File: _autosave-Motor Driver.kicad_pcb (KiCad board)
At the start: 2 copper layers, 103.6 x 67.8 mm, 45 parts, among them CON1 AVR-ISP-6, J1 Conn_01x02, J10 Conn_01x04, J2 Conn_01x02, J3 Conn_01x04, J4 Conn_01x04, J5 Conn_01x04, J6 Conn_02x02_Odd_Even, J7 Conn_01x02, J8 Conn_01x02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

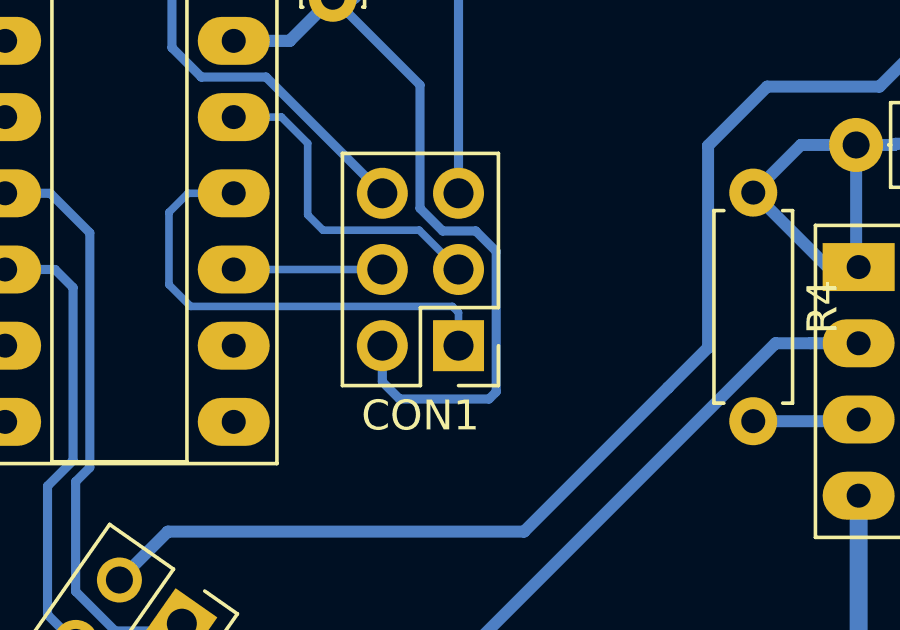
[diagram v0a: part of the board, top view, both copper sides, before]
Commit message: Updated SCH|PCB
Updated the SCh for polarity change on the fly using the 2x2 pinheader
PCB was completely newly designed
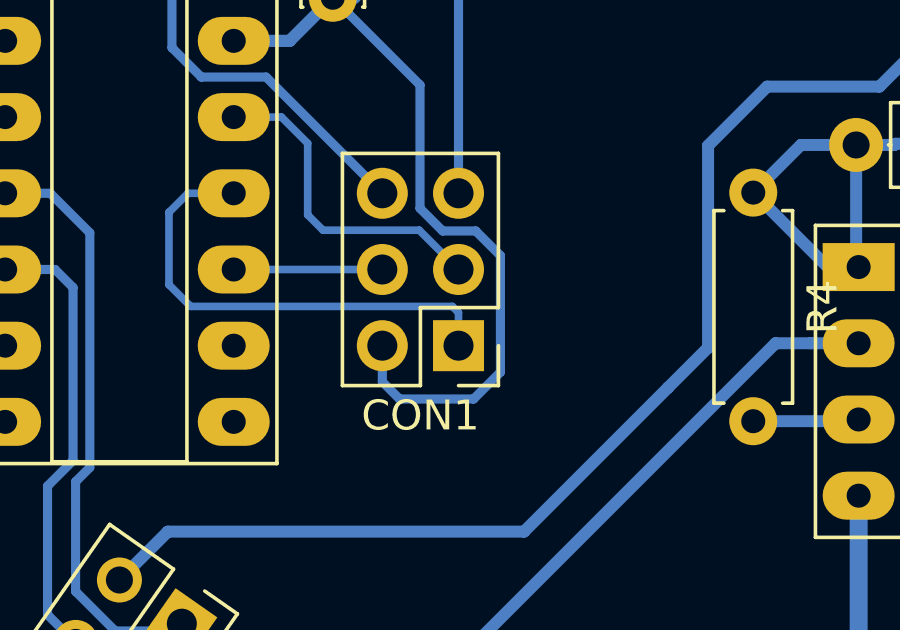
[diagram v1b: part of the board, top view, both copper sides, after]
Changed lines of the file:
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@@
     (links 111)
     (no_connects 0)
-    (area 0 0 0 0)
+    (area 90.056499 68.529999 193.788501 136.448001)
     (thickness 1.6)
     (drawings 8)
@@
   (gr_line (start 193.7385 68.58) (end 193.7385 133.096) (layer Edge.Cuts) (width 0.1))
   (gr_line (start 90.17 68.58) (end 193.7385 68.58) (layer Edge.Cuts) (width 0.1))
+  (segment (start 137.287 115.2525) (end 137.287 116.454581) (width 0.3048) (layer B.Cu) (net 1))
+  (segment (start 139.297755 111.428901) (end 138.543401 110.674547) (width 0.3048) (layer B.Cu) (net 1))
+  (segment (start 138.543401 110.674547) (end 138.543401 106.562901) (width 0.3048) (layer B.Cu) (net 1))
+  (segment (start 137.287 116.454581) (end 137.862919 117.0305) (width 0.3048) (layer B.Cu) (net 1))
+  (segment (start 141.223171 112.249197) (end 140.402875 111.428901) (width 0.3048) (layer B.Cu) (net 1))
+  (segment (start 137.862919 117.0305) (end 140.328362 117.0305) (width 0.3048) (layer B.Cu) (net 1))
+  (segment (start 140.328362 117.0305) (end 141.223171 116.135691) (width 0.3048) (layer B.Cu) (net 1))
+  (segment (start 141.223171 116.135691) (end 141.223171 112.249197) (width 0.3048) (layer B.Cu) (net 1))
+  (segment (start 140.402875 111.428901) (end 139.297755 111.428901) (width 0.3048) (layer B.Cu) (net 1))
+  (segment (start 138.543401 106.562901) (end 135.636 103.6555) (width 0.3048) (layer B.Cu) (net 1))
   (segment (start 129.566233 90.132733) (end 129.566233 84.290733) (width 0.4) (layer B.Cu) (net 1))
   (segment (start 129.566233 84.290733) (end 128.2065 82.931) (width 0.4) (layer B.Cu) (net 1))
@@
   (segment (start 121.777131 91.10971) (end 120.65 89.982579) (width 0.4064) (layer B.Cu) (net 1))
   (segment (start 120.65 89.982579) (end 120.65 89.9795) (width 0.4064) (layer B.Cu) (net 1))
-  (segment (start 137.287 115.2525) (end 137.287 116.454581) (width 0.3048) (layer B.Cu) (net 1))
-  (segment (start 137.287 116.454581) (end 137.862919 117.0305) (width 0.3048) (layer B.Cu) (net 1))
-  (segment (start 137.862919 117.0305) (end 140.843 117.0305) (width 0.3048) (layer B.Cu) (net 1))
-  (segment (start 140.843 117.0305) (end 141.083401 116.790099) (width 0.3048) (layer B.Cu) (net 1))
-  (segment (start 141.083401 116.790099) (end 141.083401 112.109427) (width 0.3048) (layer B.Cu) (net 1))
-  (segment (start 141.083401 112.109427) (end 140.402875 111.428901) (width 0.3048) (layer B.Cu) (net 1))
-  (segment (start 140.402875 111.428901) (end 139.297755 111.428901) (width 0.3048) (layer B.Cu) (net 1))
-  (segment (start 139.297755 111.428901) (end 138.543401 110.674547) (width 0.3048) (layer B.Cu) (net 1))
-  (segment (start 138.543401 110.674547) (end 138.543401 106.562901) (width 0.3048) (layer B.Cu) (net 1))
-  (segment (start 138.543401 106.562901) (end 135.636 103.6555) (width 0.3048) (layer B.Cu) (net 1))
   (segment (start 114.3 89.9795) (end 114.3 88.0745) (width 0.4064) (layer B.Cu) (net 1))
   (segment (start 114.3 88.0745) (end 120.015 88.0745) (width 0.4064) (layer B.Cu) (net 1))
@@
   (segment (start 139.827 114.1485) (end 139.622001 113.943501) (width 0.254) (layer B.Cu) (net 8))
   (segment (start 139.622001 113.943501) (end 130.898001 113.943501) (width 0.254) (layer B.Cu) (net 8))
-  (segment (start 139.827 112.7125) (end 138.518001 111.403501) (width 0.254) (layer B.Cu) (net 9))
-  (segment (start 138.518001 111.403501) (end 135.309558 111.403501) (width 0.254) (layer B.Cu) (net 9))
-  (segment (start 135.309558 111.403501) (end 134.798754 110.892697) (width 0.254) (layer B.Cu) (net 9))
-  (segment (start 134.798754 110.892697) (end 134.798754 108.504903) (width 0.254) (layer B.Cu) (net 9))
   (segment (start 134.798754 108.504903) (end 133.926351 107.6325) (width 0.254) (layer B.Cu) (net 9))
   (segment (start 133.926351 107.6325) (end 132.334 107.6325) (width 0.254) (layer B.Cu) (net 9))
+  (segment (start 139.827 112.7125) (end 138.518001 111.403501) (width 0.254) (layer B.Cu) (net 9))
+  (segment (start 134.798754 110.892697) (end 134.798754 108.504903) (width 0.254) (layer B.Cu) (net 9))
+  (segment (start 135.309558 111.403501) (end 134.798754 110.892697) (width 0.254) (layer B.Cu) (net 9))
+  (segment (start 138.518001 111.403501) (end 135.309558 111.403501) (width 0.254) (layer B.Cu) (net 9))
   (segment (start 137.287 112.7125) (end 132.334 112.7125) (width 0.254) (layer B.Cu) (net 10))
   (segment (start 139.827 110.1725) (end 139.827 99.177363) (width 0.3048) (layer B.Cu) (net 11))
